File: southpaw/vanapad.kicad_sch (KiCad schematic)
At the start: 143 parts, among them J3 Battery JST, J3 Battery THT, J3 External Power Switch, SW1 MX_SW_HS, SW10 MX_SW_HS, SW11 MX_SW_HS, SW12 MX_SW_HS, SW13 MX_SW_HS, SW14 MX_SW_HS, SW15 MX_SW_HS, SW16 MX_SW_HS, SW17 MX_SW_HS, SW18 MX_SW_HS, SW19 MX_SW_HS, SW2 MX_SW_HS, SW20 MX_SW_HS, SW21 MX_SW_HS, SW22 MX_SW_HS, SW23 MX_SW_HS, SW24 MX_SW_HS, SW25 MX_SW_HS, SW26 MX_SW_HS, SW27 MX_SW_HS, SW28 MX_SW_HS, SW29 MX_SW_HS, SW29 SW_Push, SW3 MX_SW_HS, SW30 MX_SW_HS, SW30 On-Board Power Switch, SW31 MX_SW_HS, SW32 MX_SW_HS, SW33 MX_SW_HS, SW34 MX_SW_HS, SW35 MX_SW_HS, SW36 MX_SW_HS, SW37 MX_SW_HS, SW38 MX_SW_HS, SW39 MX_SW_HS, SW4 MX_SW_HS, SW40 MX_SW_HS, SW41 MX_SW_HS, SW42 MX_SW_HS, SW43 MX_SW_HS, SW44 MX_SW_HS, SW45 MX_SW_HS, SW46 MX_SW_HS, SW47 MX_SW_HS, SW48 MX_SW_HS, SW49 MX_SW_HS, SW5 MX_SW_HS, SW50 MX_SW_HS, SW51 MX_SW_HS, SW52 MX_SW_HS, SW53 MX_SW_HS, SW54 MX_SW_HS, SW55 MX_SW_HS, SW56 MX_SW_HS, SW57 MX_SW_HS, SW58 MX_SW_HS, SW59 MX_SW_HS, SW6 MX_SW_HS, SW60 MX_SW_HS, SW61 MX_SW_HS, SW64 MX_SW_HS, SW65 MX_SW_HS, SW66 MX_SW_HS, SW67 MX_SW_HS, SW7 MX_SW_HS, SW8 MX_SW_HS, SW9 MX_SW_HS, U1 nice_nano

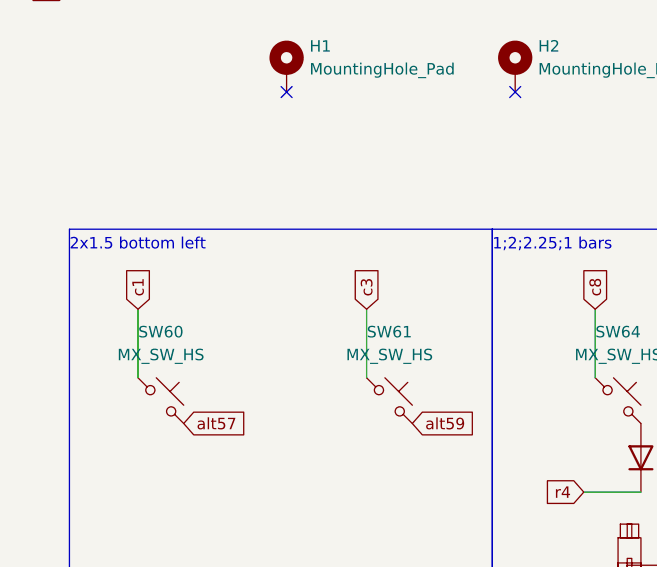
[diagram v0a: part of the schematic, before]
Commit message: fix alternative bottom row routing
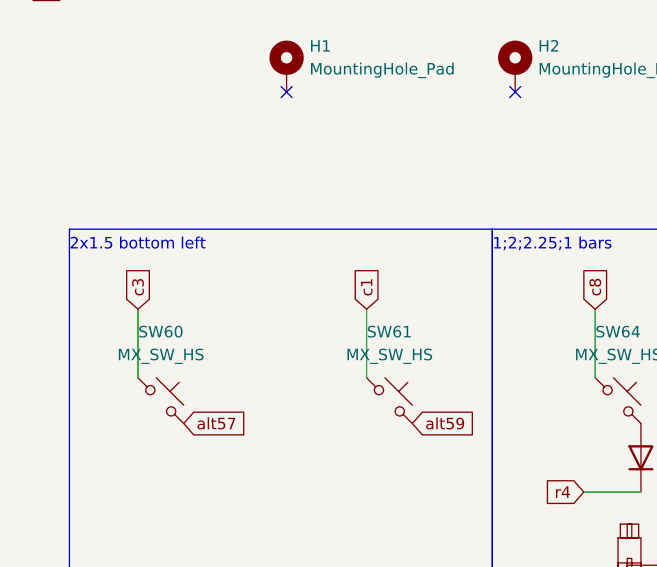
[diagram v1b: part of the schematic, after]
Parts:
- SW60, SW61: footprint PCM_marbastlib-mx:SW_MX_HS_1u -> PCM_marbastlib-mx:SW_MX_HS_CPG151101S11_1.5u
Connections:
- net c1: now also SW61.1; no longer SW60.1
- net c3: now also SW60.1; no longer SW61.1
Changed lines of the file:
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@@
 		)
 	)
+	(global_label "c1"
+		(shape input)
+		(at 54.61 156.21 90)
+		(fields_autoplaced yes)
+		(effects
+			(font
+				(size 1.27 1.27)
+			)
+			(justify left)
+		)
+		(property "Intersheetrefs" "${INTERSHEET_REFS}"
+			(at 54.61 150.9267 90)
+			(effects
+				(font
+					(size 1.27 1.27)
+				)
+				(justify left)
+				(hide yes)
+			)
+		)
+	)
 	(global_label "r6"
 		(shape input)
@@
 		)
 	)
+	(global_label "c3"
+		(shape input)
+		(at 29.21 156.21 90)
+		(fields_autoplaced yes)
+		(effects
+			(font
+				(size 1.27 1.27)
+			)
+			(justify left)
+		)
+		(property "Intersheetrefs" "${INTERSHEET_REFS}"
+			(at 29.21 150.9267 90)
+			(effects
+				(font
+					(size 1.27 1.27)
+				)
+				(justify left)
+				(hide yes)
+			)
+		)
+	)
 	(global_label "vbat"
 		(shape input)
@@
 		)
 	)
-	(global_label "c3"
-		(shape input)
-		(at 54.61 156.21 90)
-		(fields_autoplaced yes)
-		(effects
-			(font
-				(size 1.27 1.27)
-			)
-			(justify left)
-		)
-		(property "Intersheetrefs" "${INTERSHEET_REFS}"
-			(at 54.61 150.9267 90)
-			(effects
-				(font
-					(size 1.27 1.27)
-				)
-				(justify left)
-				(hide yes)
-			)
-		)
-	)
 	(global_label "bat+"
 		(shape input)
@@
 	(global_label "c1"
 		(shape input)
-		(at 29.21 156.21 90)
-		(fields_autoplaced yes)
-		(effects
-			(font
-				(size 1.27 1.27)
-			)
-			(justify left)
-		)
-		(property "Intersheetrefs" "${INTERSHEET_REFS}"
-			(at 29.21 150.9267 90)
-			(effects
-				(font
-					(size 1.27 1.27)
-				)
-				(justify left)
-				(hide yes)
-			)
-		)
-	)
-	(global_label "c1"
-		(shape input)
 		(at 24.13 24.13 90)
 		(fields_autoplaced yes)
@@
 			)
 		)
-		(property "Footprint" "PCM_marbastlib-mx:SW_MX_HS_1u"
+		(property "Footprint" "PCM_marbastlib-mx:SW_MX_HS_CPG151101S11_1.5u"
 			(at 31.75 166.37 0)
 			(effects
@@
 			)
 		)
-		(property "Footprint" "PCM_marbastlib-mx:SW_MX_HS_1u"
+		(property "Footprint" "PCM_marbastlib-mx:SW_MX_HS_CPG151101S11_1.5u"
 			(at 57.15 166.37 0)
 			(effects

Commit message: feat: add vanapad plate
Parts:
- renumbered J3 to J1, J3 to J2, SW30 to SW62, SW29 to SW63
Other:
- note added: "2x1.5 bottom right"
- note removed: "2x1.5 bottom left"
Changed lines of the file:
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@@
 (kicad_sch
-	(version 20231120)
+	(version 20250114)
 	(generator "eeschema")
-	(generator_version "8.0")
+	(generator_version "9.0")
 	(paper "A4")
+	(rectangle
+		(start 68.58 147.32)
+		(end 140.97 187.96)
+		(stroke
+			(width 0)
+			(type default)
+		)
+		(fill
+			(type none)
+		)
+	)
+	(rectangle
+		(start 21.59 147.32)
+		(end 68.58 187.96)
+		(stroke
+			(width 0)
+			(type default)
+		)
+		(fill
+			(type none)
+		)
+	)
+	(rectangle
+		(start 58.42 16.51)
+		(end 71.12 73.66)
+		(stroke
+			(width 0)
+			(type default)
+		)
+		(fill
+			(type none)
+		)
+	)
+	(text "1;2;2.25;1 bars"
+		(exclude_from_sim no)
+		(at 68.58 149.86 0)
+		(effects
+			(font
+				(size 1.27 1.27)
+			)
+			(justify left bottom)
+		)
+	)
+	(text "2x1.5 bottom right"
+		(exclude_from_sim no)
+		(at 21.59 149.86 0)
+		(effects
+			(font
+				(size 1.27 1.27)
+			)
+			(justify left bottom)
+		)
+	)
 	(junction
 		(at 67.31 120.65)
@@
 		)
 	)
-	(rectangle
-		(start 68.58 147.32)
-		(end 140.97 187.96)
-		(stroke
-			(width 0)
-			(type default)
-		)
-		(fill
-			(type none)
-		)
-	)
-	(rectangle
-		(start 21.59 147.32)
-		(end 68.58 187.96)
-		(stroke
-			(width 0)
-			(type default)
-		)
-		(fill
-			(type none)
-		)
-	)
-	(rectangle
-		(start 58.42 16.51)
-		(end 71.12 73.66)
-		(stroke
-			(width 0)
-			(type default)
-		)
-		(fill
-			(type none)
-		)
-	)
-	(text "1;2;2.25;1 bars"
-		(exclude_from_sim no)
-		(at 68.58 149.86 0)
-		(effects
-			(font
-				(size 1.27 1.27)
-			)
-			(justify left bottom)
-		)
-	)
-	(text "2x1.5 bottom left"
-		(exclude_from_sim no)
-		(at 21.59 149.86 0)
-		(effects
-			(font
-				(size 1.27 1.27)
-			)
-			(justify left bottom)
-		)
-	)
 	(global_label "gnd"
 		(shape input)
@@
 		(dnp no)
 		(fields_autoplaced yes)
-		(property "Reference" "SW30"
+		(property "Reference" "SW62"
 			(at 261.62 21.59 0)
 			(effects
@@
 		(dnp no)
 		(fields_autoplaced yes)
-		(property "Reference" "J3"
+		(property "Reference" "J2"
 			(at 264.16 40.64 0)
 			(effects
@@
 		(dnp no)
 		(fields_autoplaced yes)
-		(property "Reference" "SW29"
+		(property "Reference" "SW63"
 			(at 261.62 57.15 0)
 			(effects
@@
 		(dnp no)
 		(fields_autoplaced yes)
-		(property "Reference" "J3"
+		(property "Reference" "J1"
 			(at 264.16 77.47 0)
 			(effects
@@
 		)
 	)
+	(embedded_fonts no)
 )
